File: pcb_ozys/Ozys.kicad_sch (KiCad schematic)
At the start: 24 parts, among them CN1 532610571, J2 5037630491, U4 ISO1044BD, U5 STM32F412RETx, U6 MKDV32GCL-STP, U7 W25Q512JVFIQ, X1 X322516MLB4SI

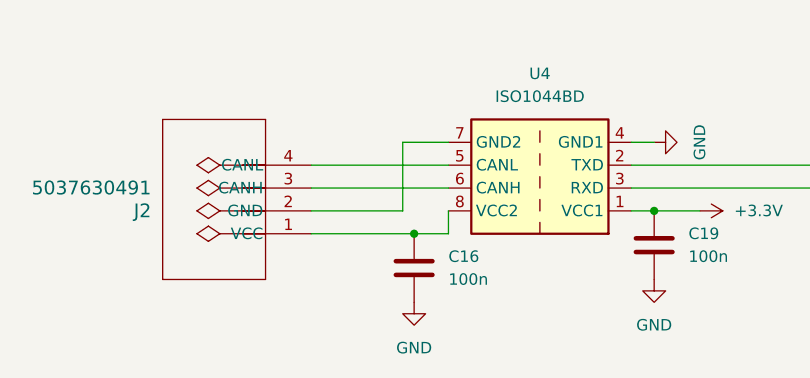
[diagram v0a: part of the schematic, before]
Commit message: Started PCBs fixed connectors
- Fixed Bypass on CAN
- Seperated SG connectors from 2x1 to 1x1
- Rough Draft of Epsilon
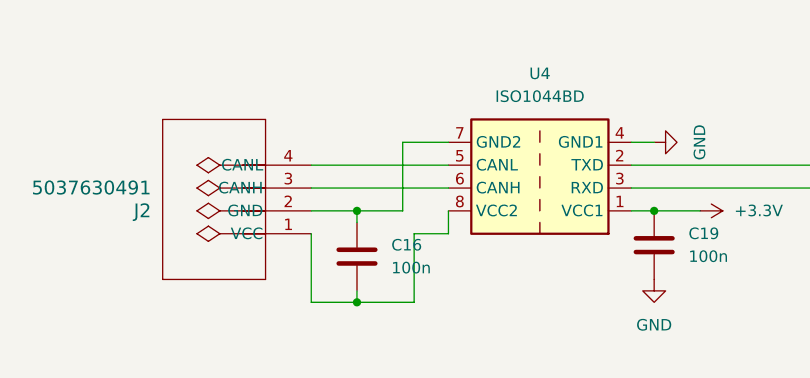
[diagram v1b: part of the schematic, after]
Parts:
- J2: footprint CON_5037630491 -> Rocketry_Manual:CON_5037630491
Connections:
- net GND: no longer C16.2
- net at J2.1 (VCC), U4.8 (VCC2): now also C16.2; no longer C16.1
- net at J2.2 (GND), U4.7 (GND2): now also C16.1
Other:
- moved on the sheet: C16
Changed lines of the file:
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@@
 	)
 	(junction
+		(at 54.61 158.75)
+		(diameter 0)
+		(color 0 0 0 0)
+	)
+	(junction
 		(at 162.56 140.97)
 		(diameter 0)
@@
 	)
 	(junction
-		(at 60.96 161.29)
+		(at 54.61 168.91)
 		(diameter 0)
 		(color 0 0 0 0)
@@
 	(wire
 		(pts
+			(xy 60.96 168.91) (xy 60.96 161.29)
+		)
+		(stroke
+			(width 0)
+			(type default)
+		)
+	)
+	(wire
+		(pts
 			(xy 62.23 86.36) (xy 62.23 72.39)
 		)
@@
 	(wire
 		(pts
+			(xy 49.53 168.91) (xy 54.61 168.91)
+		)
+		(stroke
+			(width 0)
+			(type default)
+		)
+	)
+	(wire
+		(pts
 			(xy 130.81 95.25) (xy 157.48 95.25)
 		)
@@
 	(wire
 		(pts
+			(xy 54.61 158.75) (xy 54.61 160.02)
+		)
+		(stroke
+			(width 0)
+			(type default)
+		)
+	)
+	(wire
+		(pts
 			(xy 82.55 113.03) (xy 85.09 113.03)
 		)
@@
 	(wire
 		(pts
-			(xy 49.53 161.29) (xy 60.96 161.29)
-		)
-		(stroke
-			(width 0)
-			(type default)
-		)
-	)
-	(wire
-		(pts
 			(xy 172.72 146.05) (xy 179.07 146.05)
 		)
@@
 	(wire
 		(pts
+			(xy 54.61 158.75) (xy 59.69 158.75)
+		)
+		(stroke
+			(width 0)
+			(type default)
+		)
+	)
+	(wire
+		(pts
 			(xy 138.43 118.11) (xy 138.43 156.21)
 		)
@@
 	(wire
 		(pts
+			(xy 49.53 168.91) (xy 49.53 161.29)
+		)
+		(stroke
+			(width 0)
+			(type default)
+		)
+	)
+	(wire
+		(pts
 			(xy 190.5 68.58) (xy 147.32 68.58)
 		)
@@
 	(wire
 		(pts
-			(xy 49.53 158.75) (xy 59.69 158.75)
+			(xy 54.61 168.91) (xy 60.96 168.91)
+		)
+		(stroke
+			(width 0)
+			(type default)
+		)
+	)
+	(wire
+		(pts
+			(xy 49.53 158.75) (xy 54.61 158.75)
 		)
 		(stroke
@@
 	(wire
 		(pts
+			(xy 54.61 167.64) (xy 54.61 168.91)
+		)
+		(stroke
+			(width 0)
+			(type default)
+		)
+	)
+	(wire
+		(pts
 			(xy 265.43 30.48) (xy 255.27 30.48)
 		)
@@
 			)
 		)
-		(property "Footprint" "CON_5037630491"
+		(property "Footprint" "Rocketry_Manual:CON_5037630491"
 			(at 50.292 167.64 0)
 			(effects
@@
 	(symbol
 		(lib_id "Device:C")
-		(at 60.96 165.1 0)
+		(at 54.61 163.83 0)
 		(unit 1)
 		(exclude_from_sim no)
@@
 		(fields_autoplaced yes)
 		(property "Reference" "C16"
-			(at 64.77 163.8299 0)
+			(at 58.42 162.5599 0)
 			(effects
 				(font
@@
 		)
 		(property "Value" "100n"
-			(at 64.77 166.3699 0)
+			(at 58.42 165.0999 0)
 			(effects
 				(font
@@
 		)
 		(property "Footprint" "Capacitor_SMD:C_0402_1005Metric"
-			(at 61.9252 168.91 0)
+			(at 55.5752 167.64 0)
 			(effects
 				(font
@@
 		)
 		(property "Datasheet" "~"
-			(at 60.96 165.1 0)
+			(at 54.61 163.83 0)
 			(effects
 				(font
@@
 		)
 		(property "Description" "Unpolarized capacitor"
-			(at 60.96 165.1 0)
+			(at 54.61 163.83 0)
 			(effects
 				(font
@@
 					(unit 1)
 				)
-			)
-		)
-	)
-	(symbol
-		(lib_id "power:GND")
-		(at 60.96 168.91 0)
-		(mirror y)
-		(unit 1)
-		(exclude_from_sim no)
-		(in_bom yes)
-		(on_board yes)
-		(dnp no)
-		(property "Reference" "#PWR047"
-			(at 60.96 175.26 0)
-			(effects
-				(font
-					(size 1.27 1.27)
-				)
-				(hide yes)
-			)
-		)
-		(property "Value" "GND"
-			(at 60.96 173.99 0)
-			(effects
-				(font
-					(size 1.27 1.27)
-				)
-			)
-		)
-		(property "Footprint" ""
-			(at 60.96 168.91 0)
-			(effects
-				(font
-					(size 1.27 1.27)
-				)
-				(hide yes)
-			)
-		)
-		(property "Datasheet" ""
-			(at 60.96 168.91 0)
-			(effects
-				(font
-					(size 1.27 1.27)
-				)
-				(hide yes)
-			)
-		)
-		(property "Description" "Power symbol creates a global label with name \"GND\" , ground"
-			(at 60.96 168.91 0)
-			(effects
-				(font
-					(size 1.27 1.27)
-				)
-				(hide yes)
-			)
-		)
-		(pin "1"
-		)
-		(instances
-			(project "SG_PCB_V3_1"
-				(path "/c13c867e-6e7c-48dd-82ed-469b98ba6beb/f6677e1d-2e58-46fd-b64d-3824f7e6308f"
-					(reference "#PWR047")
-					(unit 1)
-				)

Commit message: Updated Epsilon PCB and Ozys Sch
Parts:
- removed C38: 1u, Capacitor_SMD:C_0402_1005Metric, symbol Device:C
- removed C39, C40: 100n, Capacitor_SMD:C_0402_1005Metric, symbol Device:C
- removed R54: 33K, Resistor_SMD:R_0402_1005Metric, symbol Device:R
- removed U7: W25Q512JVFIQ, Rocketry_Easyeda:SOIC-16_L10.3-W7.5-P1.27-LS10.4-BL, symbol Rocketry_Easyeda:W25Q512JVFIQ
- added C15: 4.7u, Capacitor_SMD:C_0402_1005Metric, symbol Device:C
- added R20, R21, R22, R9: 33K, Resistor_SMD:R_0402_1005Metric, symbol Device:R
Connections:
- net +3.3V: now also C15.2, R20.1, R21.1, R22.1, R9.1
- net +3V3A: no longer U5.1 (VBAT)
- net CS: now also R20.2
- net GND: now also C15.1
- net MKDV32_Input: now also R22.2
- net MKDV32_Ouput: now also R21.2
- net Receiver_2/EEPROM_MCU: no longer U5.41 (PA8)
- net Receiver_2/LED_SW: no longer U5.42 (PA9)
- net Receiver_3/EEPROM_MCU: no longer U5.9 (PC1)
- net Receiver_3/LED_SW: no longer U5.10 (PC2)
- net Receiver_4/EEPROM_MCU: no longer U5.37 (PC6)
- net Receiver_4/LED_SW: no longer U5.38 (PC7)
- net RECEIVER_1.OUT: now reaches U5.14 (PA0)
- net RECEIVER_1.EEPROM: now reaches U5.15 (PA1)
- net MKDV32_Clock: now reaches U5.21 (PA5), U6.3 (CLK)
- net at U6.1 (DAT2): now also R9.2
- net ADC2 renamed RECEIVER_1.LED_SW
- net ADC3: no longer names the net of U5.11 (PC3)
- net ADC4: no longer names the net of U5.25 (PC5)
- net Power/3V3A_EN: no longer names the net of U5.36 (PB15)
- net Power/PS renamed RECEIVER_2{OUT EEPROM LED_SW}
- net Receiver_Main/EEPROM_MCU: no longer names the net of U5.58 (PB6)
- net Receiver_Main/LED_SW: no longer names the net of U5.59 (PB7)
- net Receiver_Main/Receiver_Out: no longer names the net of U5.26 (PB0)
- new net Power/VBUS: U5.42 (PA9)
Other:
- sheet Receiver_1 renamed Receiver_Main
- sheet Power ports: added VBUS; removed 3V3A_EN
- sheet Receiver_2: file Receiver_1.kicad_sch -> Receiver_Extra.kicad_sch
- sheet Receiver_3: file Receiver_1.kicad_sch -> Receiver_Extra.kicad_sch
- sheet Receiver_4: file Receiver_1.kicad_sch -> Receiver_Extra.kicad_sch
- sheet Receiver_Main: file Receiver_1.kicad_sch -> Receiver_Main.kicad_sch
- moved on the sheet: C16, C17, C18, C19, C20, C21, C22, C24, C25, C26, C36, C37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
